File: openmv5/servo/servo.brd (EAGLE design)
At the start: 35.6 x 26.7 mm, 77 parts, among them IC1 TPS613222ADBVR, IC2 AP64060WU-7, IC3 LM321LVIDCKR, IC4 74LVC1G07GW,125, J1 OPENMV5-TOP, J2 1771088, K1 IMC03TS, K2 IMC03TS, Q1 SSM3J356R,LF, Q2 2N7002KW_R1_00001, Q3 2N7002KW_R1_00001, U1 74LVC1G17SE-7

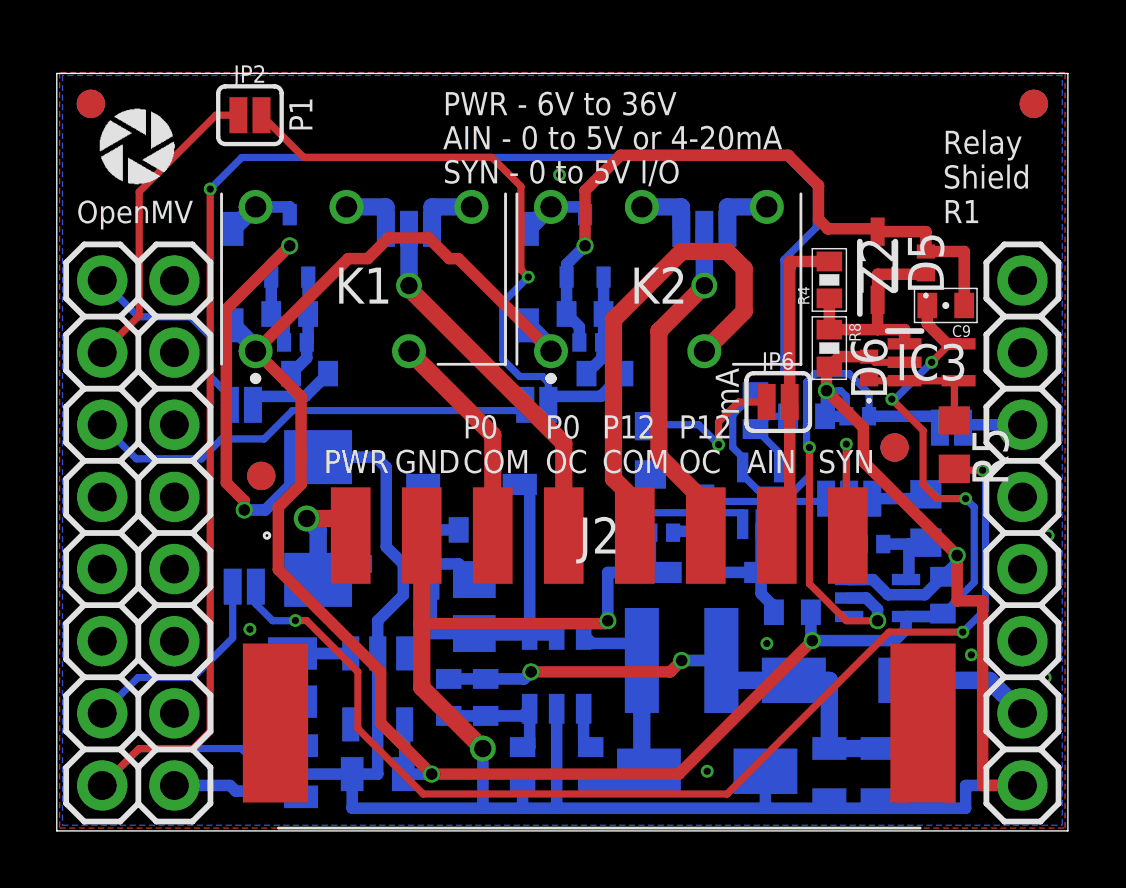
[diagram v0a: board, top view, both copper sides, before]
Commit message: Add servo shield
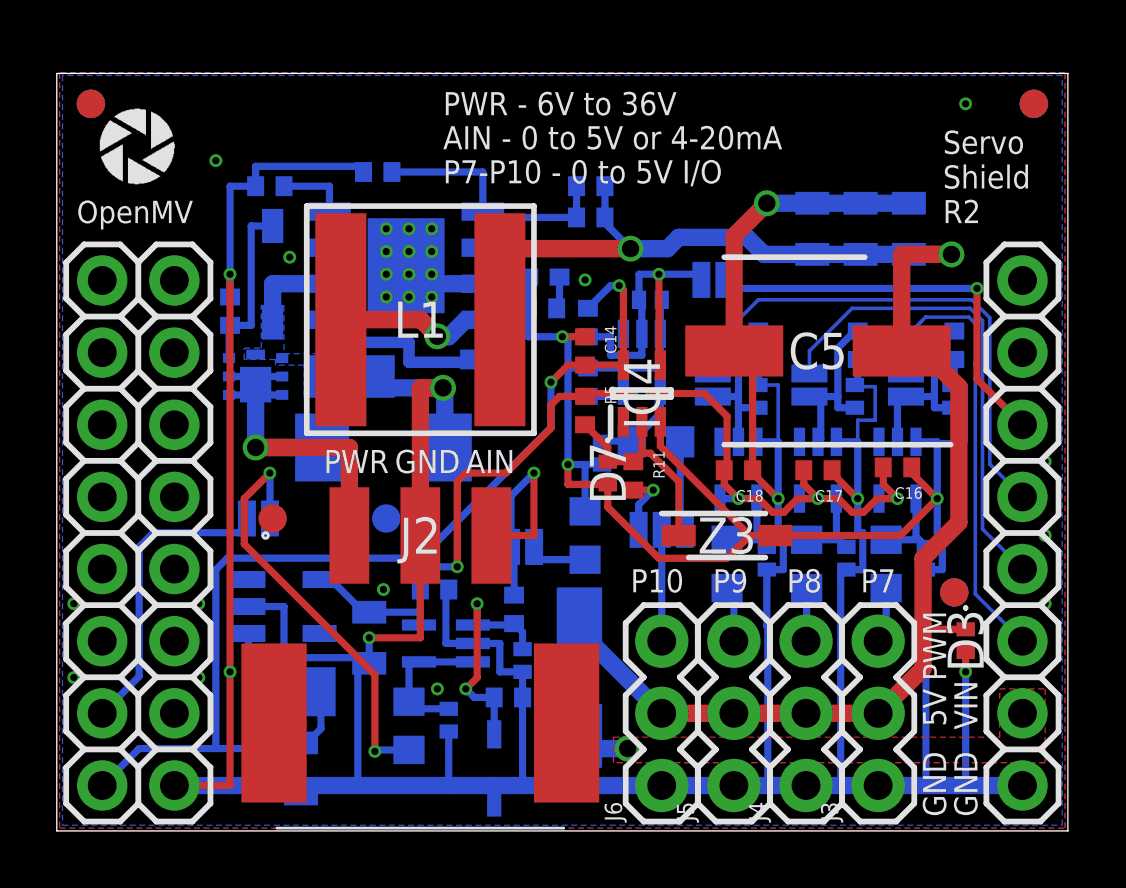
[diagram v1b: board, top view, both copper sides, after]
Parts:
- removed JP8, JP9: JUMPER-SMT_3_1-NC_PASTE_SILK, SparkFun-Jumpers:SMT-JUMPER_3_1-NC_PASTE_SILK
- removed K1, K2: IMC03TS, IMC03TS:IMC03TS
- removed Q2, Q3: 2N7002KW_R1_00001, 2N7002KW_R1_00001:SOT65P210X110-3N
- removed Z4, Z5: MMSZ5231B-7-F, MMSZ5231B-7-F:SOD3716X145N
- added C12: 2.7nF, 0402:0402
- added C13, C14, C15, C16, C17, C18: 0.1uF, 0402:0402
- added D12, D13, D14, D15: CPDQT5V0HE-HF, CPDQT5V0HE-HF:CPDQT5V0HEHF
- added J3, J4, J5, J6: (no value), SparkFun-Connectors:1X03
- added R16, R17, R18: 100K, 0402:0402
- added U2, U3, U4: 74LVC1G17SE-7, 74LVC1G17SE-7:SOT65P210X110-5N
- C1, C2: device sfe:0402-CAP -> 0402:0402
- C10: value 0.1uF -> 10nF; device sfe:0402-CAP -> 0402:0402
- C11: value 0.1uF -> 33pF; device sfe:0402-CAP -> 0402:0402
- C5: value 10uF -> EDK227M010A9HAA; device rcl:C0805 -> EDK227M010A9HAA:CAPAE660X800N
- C6: value 22uF -> 10uF; device SparkFun-Capacitors:0805 -> rcl:C0805
- C9: value 0.1uF -> 22uF; device sfe:0402-CAP -> SparkFun-Capacitors:0805
- D3: value FM240A -> CPDQT5V0HE-HF; device FM240A:DIOM5025X231N -> CPDQT5V0HE-HF:CPDQT5V0HEHF
- IC2: value AP64060WU-7 -> AP64501SP-13; device AP64060WU-7:SOT95P280X100-6N -> AP64501SP-13:SOIC127P600X163-9N
- J2: value 1771088 -> 1771033; device 1771088:1771088 -> 1771033:1771033
- JP2: value JUMPER-SMT_2_NO_SILK -> JUMPER-SMT_2_NC_PASTE_SILK; device SparkFun-Jumpers:SMT-JUMPER_2_NO_SILK -> SparkFun-Jumpers:SMT-JUMPER_2_NC_PASTE_SILK
- L1: value NRS4018T100MDGJ -> NR8040T3R6N; device NRS4018T100MDGJ:NRS4018T100MDGJ -> NR8040T3R6N:NR8040T3R6N
- Q1: value SSM3J356R,LF -> BUK6D120-60PX; device SSM3J356R_LF:SOTFL95P240X88-3N -> BUK6D120-60PX:BUK6D12060PX
- R1, R6: device sfe:0402-RES -> 0402:0402
- R10, R13: value 10K -> 470; device sfe:0402-RES -> rcl:R0603
- R11: value 240 -> 10K; device rcl:R0603 -> 0402:0402
- R12: value 10K -> 240; device sfe:0402-RES -> rcl:R0603
- R14, R15, R8: value 100K -> 470; device sfe:0402-RES -> rcl:R0603
- R2: value 22.1K -> 15.8K; device sfe:0402-RES -> 0402:0402
- R3: value 100K -> 22.1K; device sfe:0402-RES -> 0402:0402
- R4: value 51K -> 100K; device sfe:0402-RES -> 0402:0402
- R5, R9: value 470 -> 100K; device rcl:R0603 -> 0402:0402
- R7: value 100K -> 51K; device sfe:0402-RES -> 0402:0402
- moved JP2 25.0 mm to (29.9, 15.7), flipped to the bottom, turned to 270 degrees
- moved D10 23.2 mm to (31.5, 15.3), turned to 90 degrees
- moved Z2 22.3 mm to (15.4, 2.20), flipped to the bottom, turned to 270 degrees
- moved C6 21.9 mm to (10.3, 16.0), turned to 180 degrees
- moved R4 21.1 mm to (6.10, 18.3), flipped to the bottom
- moved C10 20.6 mm to (7.50, 22.7)
- moved R14 20.2 mm to (26.4, 9.40), turned to 270 degrees
- moved D5 19.9 mm to (16.4, 6.00), flipped to the bottom, turned to 270 degrees
- moved R8 19.9 mm to (12.4, 3.70), flipped to the bottom
- moved IC3 19.8 mm to (13.7, 6.60), flipped to the bottom
- moved C7 19.6 mm to (26.6, 21.2), turned to 270 degrees
- moved D6 19.3 mm to (13.8, 3.90), flipped to the bottom, turned to 270 degrees
- moved C8 19.2 mm to (28.3, 21.2), turned to 270 degrees
- moved C11 18.7 mm to (16.6, 20.0)
- moved R1 18.4 mm to (18.8, 22.7), turned to 0 degrees
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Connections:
- removed net P0: JP1.2, R12.1
- removed net P0_COM: J2.3, K1.3
- removed net P0_CONTROL: D10.1, Q2.1, R12.2, R14.2
- removed net P0_INT: J1.1, JP1.1
- removed net P0_N: J2.4, JP8.2
- removed net P0_NC: JP8.1, K1.7
- removed net P0_NO: JP8.3, K1.5
- removed net P0_RELAY: K1.8, Q2.3, Z4.2
- removed net P12: JP2.2, JP3.2, R13.1
- removed net P12_COM: J2.5, K2.3
- removed net P12_CONTROL: D11.1, Q3.1, R13.2, R15.2
- removed net P12_N: J2.6, JP9.2
- removed net P12_NC: JP9.1, K2.7
- removed net P12_NO: JP9.3, K2.5
- removed net P12_RELAY: K2.8, Q3.3, Z5.2
- removed net P1_INT: J1.2, JP2.1
- removed net P2_INT: J1.3, JP3.1
- new net EXT_VIN_COMP: C11.1, IC2.6, R2.1
- new net EXT_VIN_COMP_CAP: C12.1, R2.2
- new net EXT_VIN_SS: C10.1, IC2.4
- new net P7_PWM: D10.1, JP2.2, R16.1, U2.2
- new net P7_PWM_INT: J1.11, JP2.1
- new net P7_PWM_SERVO: J3.3, R13.2
- new net P7_PWM_SERVO_INT: D11.1, R13.1, U2.4
- new net P8_PWM: D12.1, JP3.2, R17.1, U3.2
- new net P8_PWM_INT: J1.12, JP3.1
- new net P8_PWM_SERVO: J4.3, R14.2
- new net P8_PWM_SERVO_INT: D13.1, R14.1, U3.4
- new net P9_PWM: D14.1, JP4.2, R18.1, U4.2
- new net P9_PWM_INT: J1.13, JP4.1
- new net P9_PWM_SERVO: J5.3, R15.2
- new net P9_PWM_SERVO_INT: D15.1, R15.1, U4.4
- net AIN: now also J2.3, R7.2; no longer J2.7, R4.2
- net AIN_INT: now also R7.1, R9.1; no longer R4.1, R8.1
- net AIN_OUT: now also R8.1; no longer R5.1
- net AIN_S: now also R12.2; no longer R11.2
- net EXT_VIN: now also Q1.1, Q1.2, Q1.5, Q1.6, Q1.7; no longer Q1.3
- net EXT_VIN_BST: now also C1.2; no longer C1.1
- net EXT_VIN_FB: now also IC2.5, R3.1; no longer IC2.3, R2.1
- net EXT_VIN_G: now also Q1.3, R4.1; no longer Q1.1, R3.1
- net EXT_VIN_INT: now also C6.1, IC2.2, IC2.3, Q1.4, Q1.8; no longer C5.1, IC2.4, IC2.5, Q1.2
- net EXT_VIN_OUT: now also C5.1, C9.2, D3.1, J3.2, J4.2, J5.2, J6.2; no longer C6.2
- net EXT_VIN_SW: now also C1.1, IC2.8; no longer C1.2, D3.1, IC2.6
- net GND: now also C10.2, C11.2, C12.2, C13.1, C14.1, C15.1, C16.1, C17.1, C18.1, C6.2, D12.2, D13.2, D14.2, D15.2, IC2.7, IC2.9, J3.1, J4.1, J5.1, J6.1, R12.1, R16.2, R17.2, R18.2, R4.2, R9.2, U2.3, U3.3, U4.3; no longer C10.1, C11.1, C6.1, IC2.2, Q2.2, Q3.2, R11.1, R14.1, R15.1, R2.2, R8.2
- net P10_FSYNC: now also R6.2; no longer R7.2
- net P6_ADC: now also JP1.2, R8.2; no longer JP4.2, R5.2
- net P6_ADC_INT: now also JP1.1; no longer JP4.1
- net SYNC: now also J6.3; no longer J2.8
- net SYNC_IN: now also R11.2; no longer R10.2
- net SYNC_IN_INT: now also R11.1, R5.2; no longer R10.1, R6.2
- net SYNC_OUT: now also R10.2; no longer R9.2
- net SYNC_OUT_INT: now also R10.1; no longer R9.1
- net VCC: now also C14.2, R6.1; no longer C10.2, R7.1
- net V_BATT: now also C13.2, C15.2, C16.2, C17.2, C18.2, R5.1, U2.5, U3.5, U4.5; no longer C11.2, C9.2, K1.1, K2.1, R6.1, Z4.1, Z5.1
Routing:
- net GND: track 160.8 -> 221.9 mm, vias 14 -> 36
- net V_BATT: track 73.7 -> 38.0 mm
- net EXT_VIN_OUT: track 20.2 -> 55.4 mm
- net VCC: track 67.4 -> 38.7 mm, vias 1 -> 2
- net P6_ADC: track 38.9 -> 14.9 mm, vias 3 -> 2
- net P12: track 22.5 -> 0.00 mm, vias 1 -> 0
- net P9_PWM_INT: track 0.00 -> 18.5 mm
- net P12_COM: track 17.2 -> 0.00 mm
- net P8_PWM_INT: track 0.00 -> 17.0 mm
- net P2_INT: track 16.3 -> 0.00 mm
- net P7_PWM_INT: track 0.00 -> 16.0 mm
- net P10_FSYNC: track 25.1 -> 11.0 mm, vias 2 -> 1
- net P0_N: track 13.1 -> 0.00 mm, vias 1 -> 0
- net P10_FSYNC_INT: track 2.14 -> 14.5 mm, vias 0 -> 1
- net P12_N: track 12.1 -> 0.00 mm, vias 1 -> 0
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- added copper zone on layer 16, net EXT_VIN_INT
- added copper zone on layer 1, net VIN
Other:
- board text added: "4.28.23"
- board text added: "5V"
- board text added: "P10"
- board text added: "P7"
- board text added: "P7-P10 - 0 to 5V I/O"
- board text added: "P8"
- board text added: "P9"
- board text added: "PWM"
- board text added: "Servo Shield R2"
- board text removed: "4.18.23"
- board text removed: "NC"
- board text removed: "NO"
- board text removed: "P0"
- board text removed: "P0 COM"
- board text removed: "P0 OC"
- board text removed: "P1"
- board text removed: "P12"
- board text removed: "P12 COM"
- board text removed: "P12 OC"
- board text removed: "P2"
- board text removed: "Relay Shield R1"
- board text removed: "SYN - 0 to 5V I/O"

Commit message: Remove zener diode from ADC circuit
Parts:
- Z2: value MM3Z3V6T1G -> DNP
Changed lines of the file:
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@@
 <attribute name="VALUE" x="14.305" y="4.335" size="1.27" layer="28" rot="MR270"/>
 </element>
-<element name="Z2" library="MM3Z3V6T1G" package="SOD2512X110N" value="MM3Z3V6T1G" x="15.4" y="2.2" smashed="yes" rot="MR270">
+<element name="Z2" library="MM3Z3V6T1G" package="SOD2512X110N" value="DNP" x="15.4" y="2.2" smashed="yes" rot="MR270">
 <attribute name="DESCRIPTION" value="ON Semiconductor MM3Z3V6T1G Zener Diode, 3.6V 5% 200 mW SMT 2-Pin SOD-323" x="15.4" y="2.2" size="1.778" layer="28" rot="MR270" display="off"/>
 <attribute name="HEIGHT" value="1.1mm" x="15.4" y="2.2" size="1.778" layer="28" rot="MR270" display="off"/>
@@
 <attribute name="MPN" value="MM3Z3V6T1G" x="15.4" y="2.2" size="1.778" layer="28" rot="MR270" display="off"/>
 <attribute name="NAME" x="15.4" y="2.2" size="1.27" layer="26" rot="MR270" align="center"/>
+<attribute name="POPULATE" value="0" x="15.4" y="2.2" size="1.778" layer="28" rot="MR270" display="off"/>
 <attribute name="VALUE" x="15.4" y="2.2" size="1.27" layer="28" rot="MR270" align="center"/>
 </element>
